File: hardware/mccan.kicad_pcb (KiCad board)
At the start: 6 copper layers, 140 x 100 mm, 238 parts, among them J1 PWR pigtail -> SS1.5 3w, J2 Prog/UART, J3 FL pigtail -> SS1.0 key A / b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, J4 FR pigtail -> SS1.0 key B / g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, J5 RL pigtail -> SS1.0 key C / b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, J6 RR pigtail -> SS1.0 key D / n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, J7 DENALI pigtail -> SS1.5 3w, J8 CAN pigtail -> SS1.0 2w, Q10 IPT008N06NM5LF, Q11 IPT008N06NM5LF, Q12 MMBT3904, Q2 MMBT3904, Q3 MMBT3904, Q4 NX5020UNBKS, Q5 NX5020UNBKS, Q6 NX5020UNBKS, Q7 NX5020UNBKS, Q8 NX5020UNBKS, Q9 NX5020UNBKS, SW1 BOOT, SW2 EN/RESET, U1 LM5164DDA, U10 LTC4380HMS-2, U2 LM5164DDA, U3 LM51571-Q1, U4 DML3017LDC, U5 ESP32-WROOM-32E-N8, U6 TJA1042T/3, U7 PCA9685PW/Q900, U8 ADG706, U9 BTS7008-2EPA

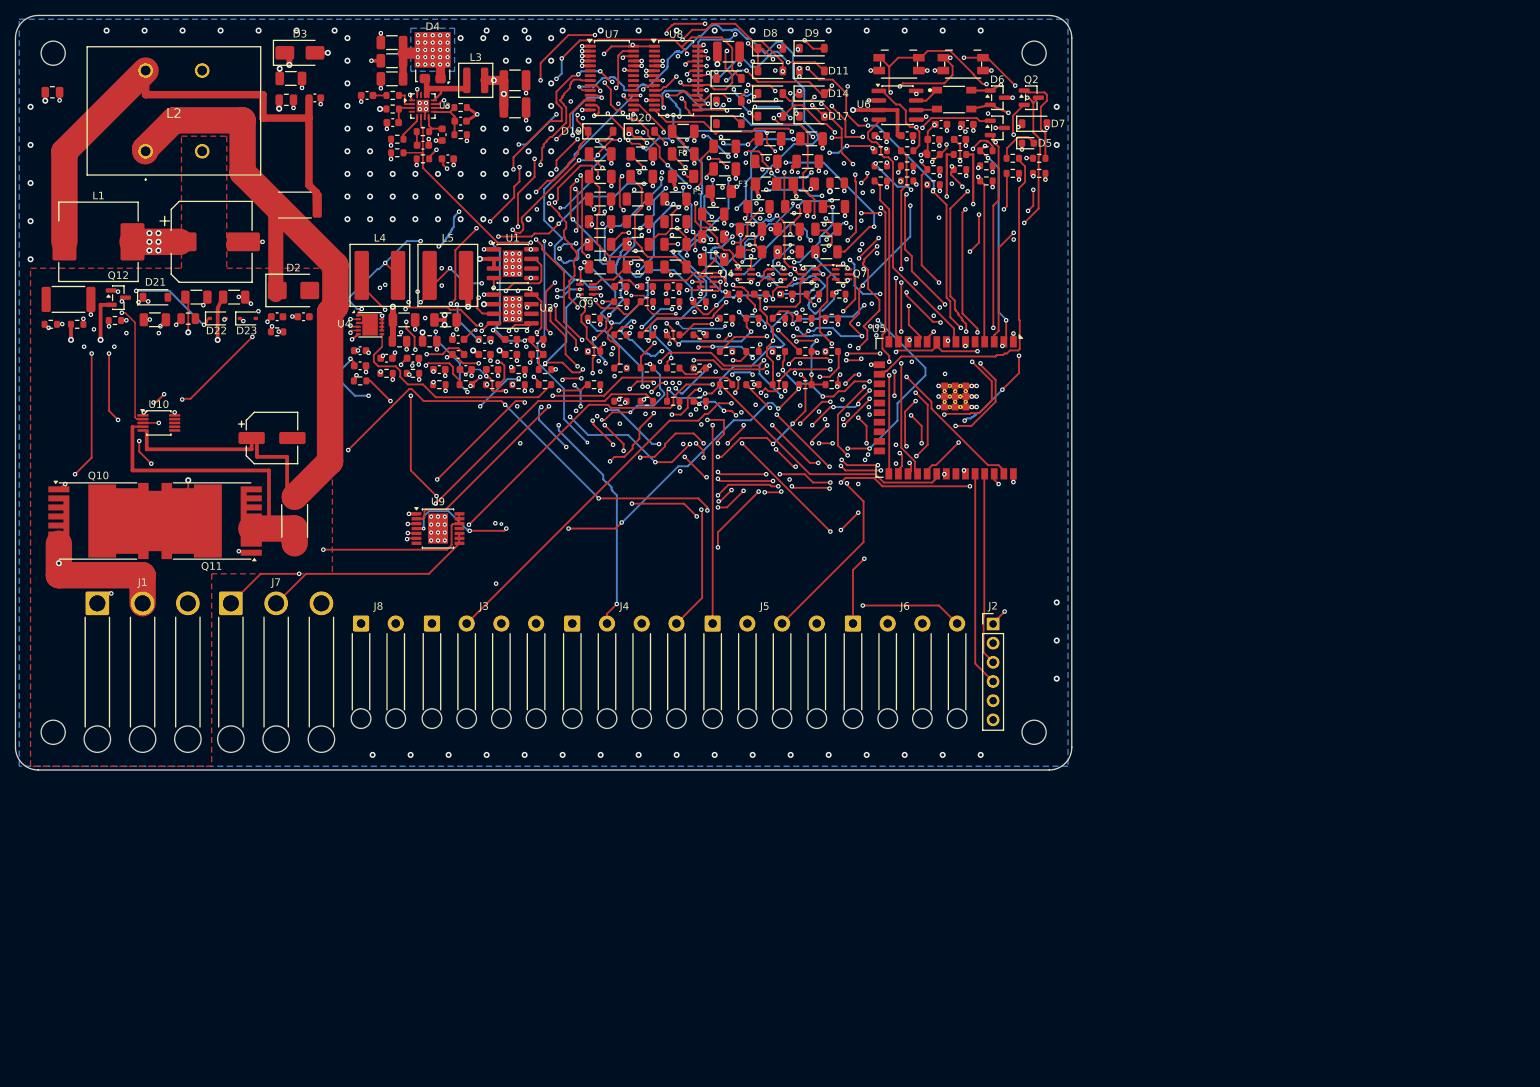
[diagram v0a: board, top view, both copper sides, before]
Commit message: hw(pcb): tear out the old copper, which the re-layout invalidates
Every hand route named absolute coordinates against a placement that is about to
change, and routes_signal.json named coordinates AND In4.Cu, which is about to stop
being a signal layer. None of it could have survived the move. The reasoning in the
old route comments is about the circuit rather than the coordinates and carries over;
it is at tag board/v2-6layer.

Co-Authored-By: Claude Opus 5 <noreply@anthropic.com>
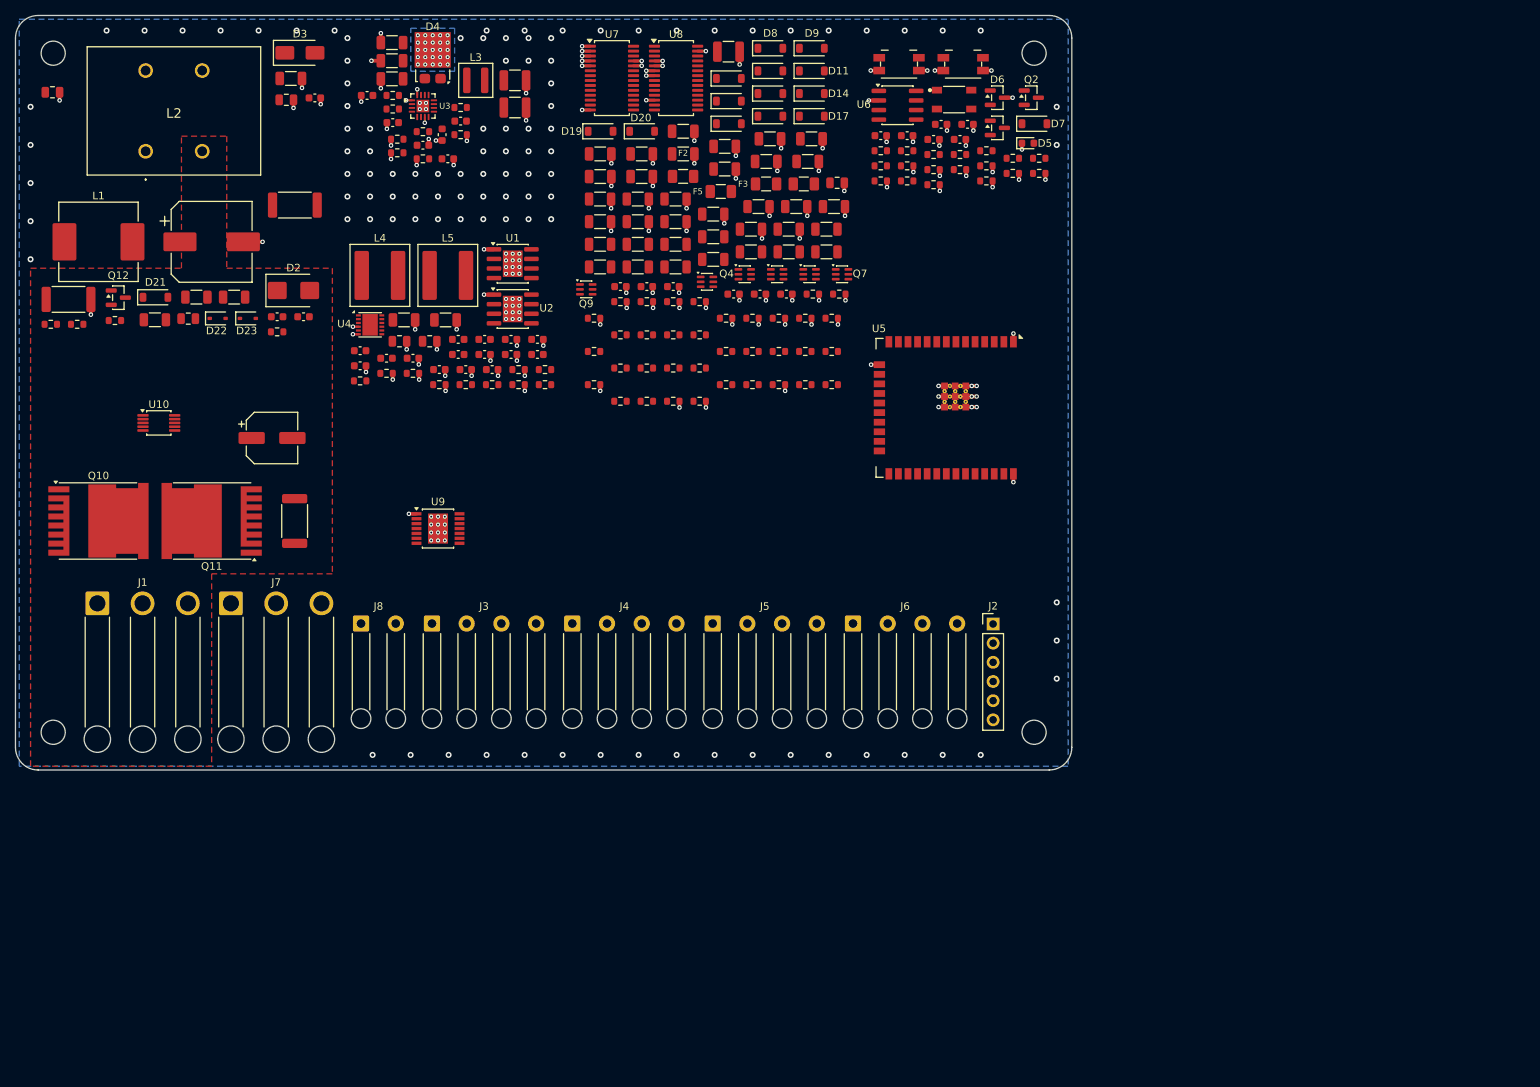
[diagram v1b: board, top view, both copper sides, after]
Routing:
- net /+3V3_SW: track 272.8 -> 0.00 mm, vias 41 -> 0
- net /+3V3_ALW: track 257.0 -> 0.00 mm, vias 31 -> 0
- net /IGN_IN: track 169.9 -> 0.00 mm, vias 14 -> 0
- net /EN_3V3SW: track 169.8 -> 0.00 mm, vias 19 -> 0
- net /CANH: track 165.6 -> 0.00 mm, vias 2 -> 0
- net /CANL: track 164.0 -> 0.00 mm, vias 2 -> 0
- net /ISNS_DEN: track 136.1 -> 0.00 mm, vias 20 -> 0
- net /outputs/+24V_FR: track 134.3 -> 0.00 mm, vias 8 -> 0
- net /outputs/PWM_RL_R: track 128.7 -> 0.00 mm, vias 11 -> 0
- net /EN_DIAG: track 125.1 -> 0.00 mm, vias 23 -> 0
- net /+5V: track 124.1 -> 0.00 mm, vias 6 -> 0
- net /outputs/RET_FR_G: track 122.2 -> 0.00 mm, vias 15 -> 0
- net /I2C_SCL: track 121.5 -> 0.00 mm, vias 16 -> 0
- net /EN_BOOST: track 114.9 -> 0.00 mm, vias 10 -> 0
- net /I2C_SDA: track 113.8 -> 0.00 mm, vias 17 -> 0
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
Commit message: hw(pcb): 200 x 140 mm, with routing channels and enforced fill budgets
Doubling the area halves the fill on its own, but it does not change the packer --
it just gives it more room to pack the same way. So the region model gains two
things it never had: 6 mm part-free channels between neighbours, which is a routing
budget that can be reasoned about rather than whatever gaps the packer left, and a
declared fill budget per region that check_density.py fails the build over.

input, the worst region on the old board, goes 75.8 % -> 38.8 %; outputs 37.3 % -> 17.1 %;
the wire-exit field 62.9 % -> 33.9 %. The comment claiming outputs was at 59 % described a
region that had been widened in the same commit, which is why this task moves the left
column rather than the right.

Co-Authored-By: Claude Opus 5 <noreply@anthropic.com>
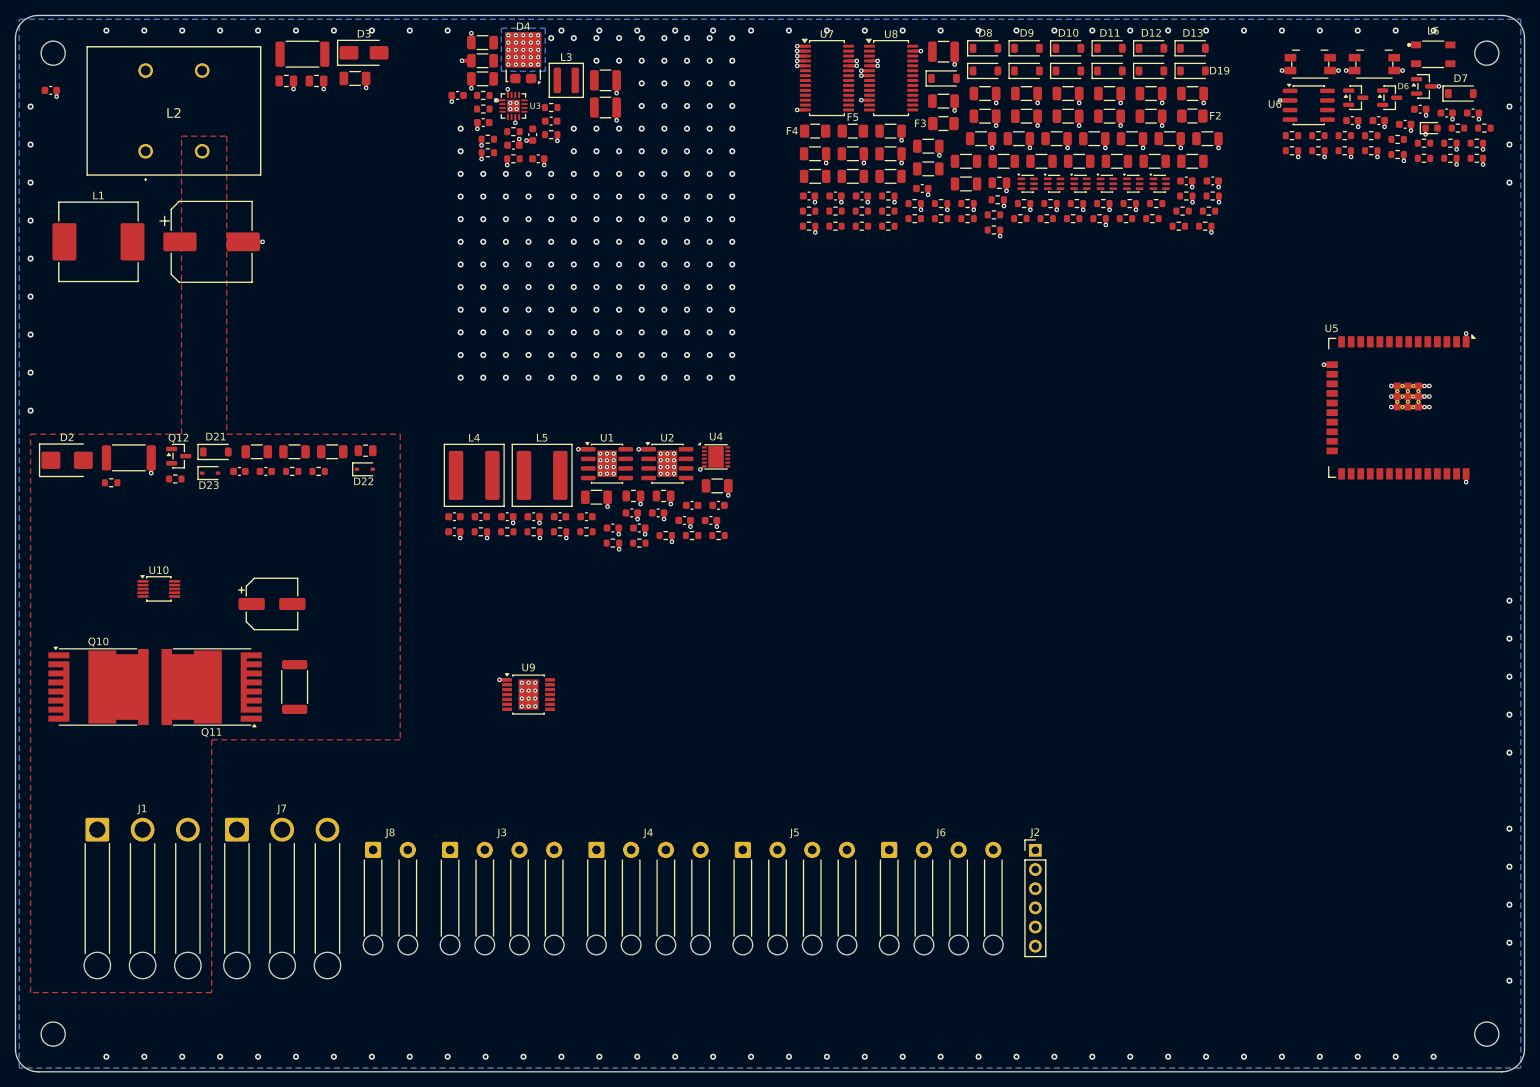
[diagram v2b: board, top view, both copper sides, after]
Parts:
- moved R59 81.2 mm to (178.0, 36.3)
- moved R42 79.7 mm to (178.7, 43.9)
- moved D19 78.9 mm to (176.1, 27.4)
- moved C37 78.6 mm to (213.2, 32.9)
- moved Q9 77.3 mm to (171.7, 42.3)
- moved R22 76.6 mm to (211.2, 34.9)
- moved R23 76.6 mm to (214.7, 34.9)
- moved C41 76.3 mm to (175.2, 41.9)
- moved C42 76.3 mm to (178.7, 41.9)
- moved R85 74.2 mm to (174.2, 47.9)
- moved R86 74.2 mm to (177.7, 47.9)
- moved C53 73.4 mm to (170.5, 30.4)
- moved C54 73.4 mm to (176.0, 30.4)
- moved R64 73.1 mm to (171.2, 44.9)
- moved H4 72.1 mm to (215.0, 155.0)
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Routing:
- net GND: track 149.6 -> 148.8 mm, vias 274 -> 435
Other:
- board size 140 x 100 mm -> 200 x 140 mm
- board text added: "Full 8-layer stackup (layer names, copper weights) lands in plan Task 5 -- this line"
- board text added: "LAYOUT CONSTRAINTS (spec 9.3, 9.4, 10 / plan Task 8), 200 x 140 mm, 8 layers"
- board text added: "TIM-A gap pad 34 x 59 mm = 2006 mm2 (B.Cu side)"
- board text added: "Was 140 x 100 mm / 6 layers until 2026-09-23 (see board outline block, layout_pcb.py)."
- board text added: "only stops the count being wrong; do not infer stackup detail from its absence here."
- board text removed: "0.20 mm clearance this board declares -- a 2 oz inner layer cannot hold it."
- board text removed: "6 layers: F.Cu sig, In1.Cu GND solid and unbroken, In2.Cu sig, In3.Cu VBAT,"
- board text removed: "In4.Cu sig, B.Cu sig. COPPER: 1 oz (35 um) on ALL SIX. 1 oz outer is what holds"
- board text removed: "LAYOUT CONSTRAINTS (spec 9.3, 9.4, 10 / plan Task 8)"
- board text removed: "TIM-A gap pad 34 x 35 mm = 1190 mm2 (B.Cu side)"
- board text removed: "U10's 0.15 mm land pattern; 1 oz inner is what lets In2/In4 be etched to the"

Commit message: hw(pcb): eight layers -- three ground planes and a split power layer
Fixes a defect the six-layer stack carried: B.Cu was a signal layer whose only
neighbour was another signal layer, so bottom-side traces had no adjacent reference
plane. A GND pour on the same layer is not a plane beneath them. Now every signal
layer has a solid GND plane on at least one face and In2.Cu has one on both, which
is where the CAN pair goes -- segregation by construction rather than by a rule
nothing enforces.

In4.Cu is split so the logic rails stop being 2.0 mm tracks. The islands are
computed from where their pads are, not drawn: the old board's hand-chosen vertical
split put seven of eleven +24V pads on the wrong side of the line. VBAT fills the
layer at priority 0 and the rails carve out of it at priority 1.

rail_island() as specified filtered pads by `pd[2] != net`, comparing pads_board()'s
net CODE against a net NAME string -- always false, so every rail island came back
empty and VBAT would have filled In4.Cu whole, split in name only. Fixed to compare
through NETNAME, the code -> name lookup every other net comparison in this file
already uses.

VBAT worst cut measured at 106.50 mm against the 11.44 mm IPC-2221 asks -- a 9.3x
margin, comfortably affordable at the default 3.0 mm rail-island halo.

Co-Authored-By: Claude Opus 5 <noreply@anthropic.com>
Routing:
- added copper zone on In4.Cu, net /+24V
- added copper zone on In4.Cu, net /+5V
- added copper zone on In4.Cu, net /VBAT
- added copper zone on In4.Cu, net /VLOGIC_IN
- added copper zone on In3.Cu, net GND
- added copper zone on In6.Cu, net GND
- removed copper zone on In3.Cu, net /VBAT
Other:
- copper layers 6 -> 8
- board text added: "F.Cu sig / In1.Cu GND / In2.Cu sig (CAN pair) / In3.Cu GND / In4.Cu POWER (split) /"
- board text added: "FEED path (7.0 A cont, 7.8 A transient): the In4.Cu polygon, /VBAT at priority 0 with"
- board text added: "In5.Cu sig / In6.Cu GND / B.Cu sig. Every signal layer has a solid GND plane on at"
- board text added: "STACKUP (1.6 mm, 1 oz throughout, see gen_pcb.STACKUP for the full dielectric table):"
- board text added: "against the 11.44 mm IPC-2221 asks (10 C rise, internal, 1 oz) -- see"
- board text added: "gen_pcb.rail_island) -- not a hand-drawn split. Measured at 106.50 mm on its worst cut"
- board text added: "least one face, and In2.Cu (CAN) has one on both -- a buried stripline by construction."
- board text added: "scripts/check_plane_width.py. On F.Cu the FEED class floor is"
- board text added: "the +24V / +5V / +VLOGIC_IN rails carved out as pad-bounded islands at priority 1 (see"
- board text removed: "FEED path (7.0 A cont, 7.8 A transient): the In3.Cu polygon, measured at 71 mm on"
- board text removed: "Full 8-layer stackup (layer names, copper weights) lands in plan Task 5 -- this line"
- board text removed: "its worst cut against the 11.44 mm IPC-2221 asks (10 C rise, internal, 1 oz) --"
- board text removed: "only stops the count being wrong; do not infer stackup detail from its absence here."
- board text removed: "see scripts/check_plane_width.py. On F.Cu the FEED class floor is"
